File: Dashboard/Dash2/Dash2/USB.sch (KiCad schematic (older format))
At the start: 8 parts, among them J501 USB_B_Micro, U501 CP2102N-A01-GQFN24

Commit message: Add complete layout of the board
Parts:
- C501: Mouser Part Number (none) -> 80-C0805C475K3RAUTO
- C502: Mouser Part Number (none) -> 80-C0805C104K3R
- D501: Mouser Part Number (none) -> 576-SP0503BAHTG
- J501: Mouser Part Number (none) -> 538-105017-1001
- R501: Mouser Part Number (none) -> 71-CRCW0805-22.1K-E3
- R502: Mouser Part Number (none) -> 71-CRCW0805-47.5K-E3
- R503: Mouser Part Number (none) -> 71-CRCW08051K00FKEAC
- U501: Mouser Part Number (none) -> 634-CP2102NA01GQFN24
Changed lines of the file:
@@
 EESchema Schematic File Version 4
-LIBS:Dash2-cache
-EELAYER 26 0
+EELAYER 30 0
 EELAYER END
 $Descr A4 11693 8268
 encoding utf-8
-Sheet 5 4
+Sheet 4 4
 Title ""
 Date ""
@@
 F 2 "Package_DFN_QFN:QFN-24-1EP_4x4mm_P0.5mm_EP2.6x2.6mm" H 5950 3000 50  0001 L CNN
 F 3 "http://www.silabs.com/support%20documents/technicaldocs/cp2102n-datasheet.pdf" H 5550 2750 50  0001 C CNN
+F 4 "634-CP2102NA01GQFN24 " H 5500 3800 50  0001 C CNN "Mouser Part Number"
 	1    5500 3800
 	1    0    0    -1
@@
 F 3 "~" H 3150 4250 50  0001 C CNN
 F 4 "105017-1001" H 3000 4300 50  0001 C CNN "P/N"
+F 5 " 538-105017-1001 " H 3000 4300 50  0001 C CNN "Mouser Part Number"
 	1    3000 4300
 	1    0    0    -1
@@
 F 2 "Package_TO_SOT_SMD:SOT-143" H 4175 4750 50  0001 L CNN
 F 3 "http://www.littelfuse.com/~/media/files/littelfuse/technical%20resources/documents/data%20sheets/sp05xxba.pdf" H 4075 4925 50  0001 C CNN
+F 4 "576-SP0503BAHTG " H 3950 4800 50  0001 C CNN "Mouser Part Number"
 	1    3950 4800
 	1    0    0    -1
@@
 F 2 "Resistor_SMD:R_0805_2012Metric" V 4630 4500 50  0001 C CNN
 F 3 "~" H 4700 4500 50  0001 C CNN
+F 4 "71-CRCW0805-47.5K-E3" H 4700 4500 50  0001 C CNN "Mouser Part Number"
 	1    4700 4500
 	1    0    0    -1
@@
 F 2 "Resistor_SMD:R_0805_2012Metric" V 4280 4100 50  0001 C CNN
 F 3 "~" H 4350 4100 50  0001 C CNN
+F 4 "71-CRCW0805-22.1K-E3" H 4350 4100 50  0001 C CNN "Mouser Part Number"
 	1    4350 4100
 	0    1    1    0
@@
 F 2 "Resistor_SMD:R_0805_2012Metric" V 4730 3000 50  0001 C CNN
 F 3 "~" H 4800 3000 50  0001 C CNN
+F 4 "71-CRCW08051K00FKEAC" H 4800 3000 50  0001 C CNN "Mouser Part Number"
 	1    4800 3000
 	1    0    0    -1
@@
 F 2 "Capacitor_SMD:C_0805_2012Metric" H 5938 2650 50  0001 C CNN
 F 3 "~" H 5900 2800 50  0001 C CNN
+F 4 "80-C0805C475K3RAUTO " H 5900 2800 50  0001 C CNN "Mouser Part Number"
 	1    5900 2800
 	1    0    0    -1
@@
 F 2 "Capacitor_SMD:C_0805_2012Metric" H 6438 2650 50  0001 C CNN
 F 3 "~" H 6400 2800 50  0001 C CNN
+F 4 "80-C0805C104K3R " H 6400 2800 50  0001 C CNN "Mouser Part Number"
 	1    6400 2800
 	1    0    0    -1

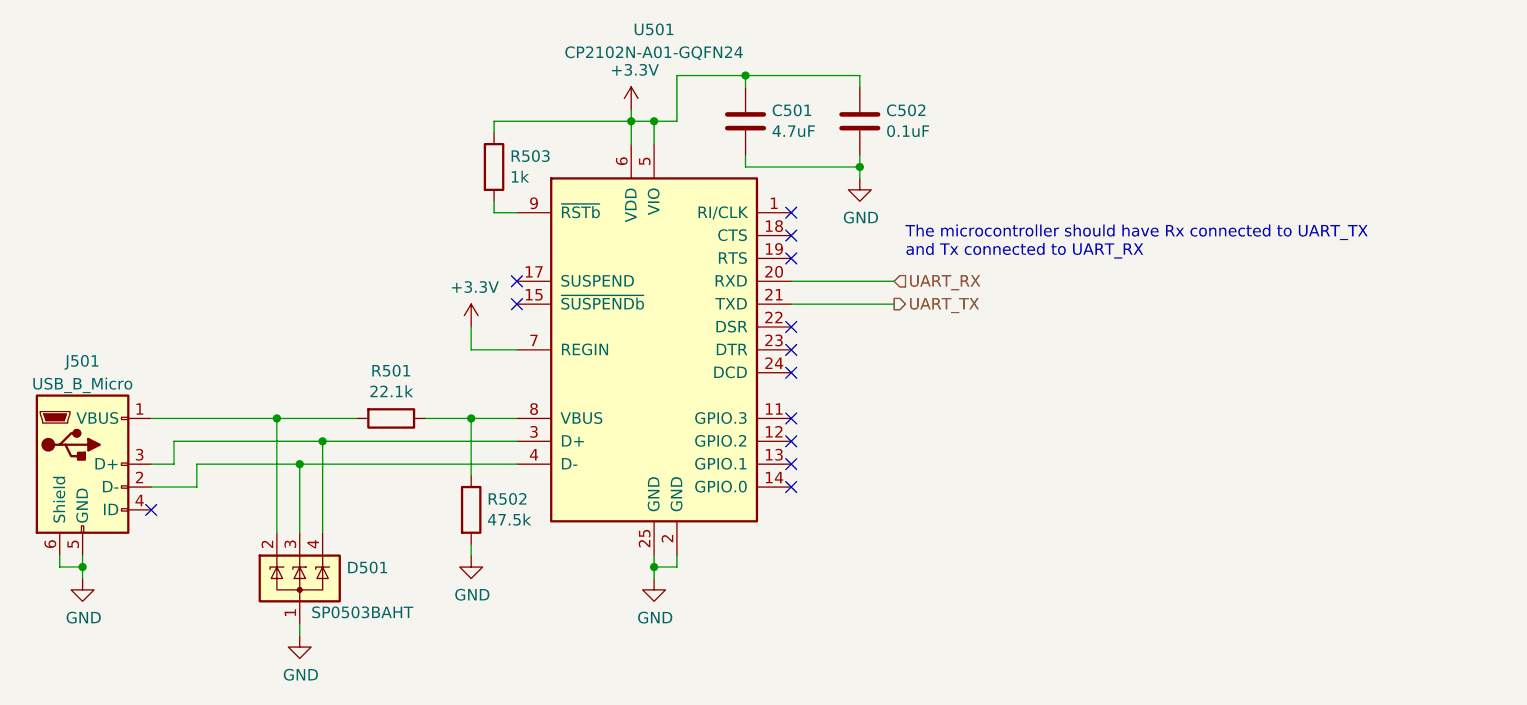
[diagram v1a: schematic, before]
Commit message: Add LED board and timing circuitry. The LED board is not yet integrated with the Dash.
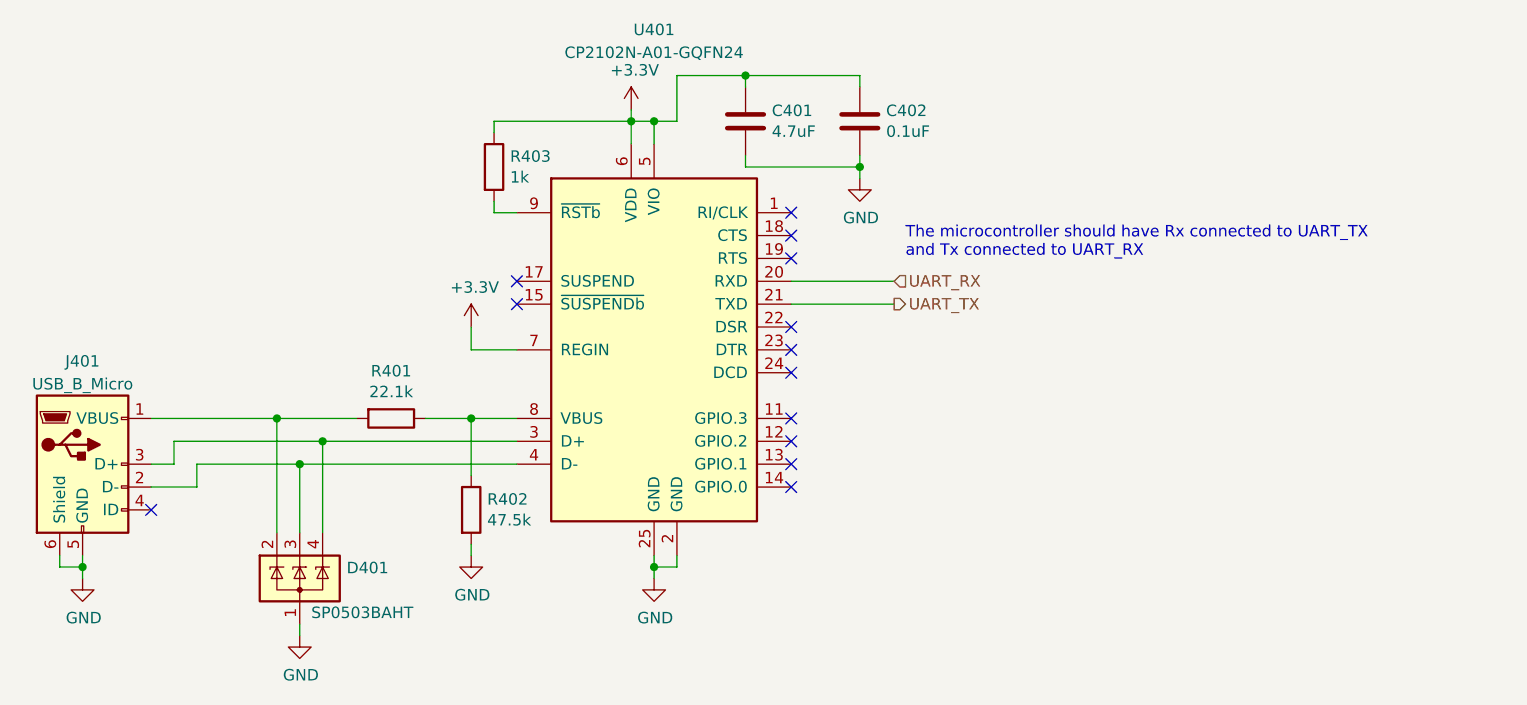
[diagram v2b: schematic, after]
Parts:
- renumbered C501 to C401, C502 to C402, D501 to D401, J501 to J401, R501 to R401, R502 to R402, R503 to R403, U501 to U401
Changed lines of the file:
@@
 $Descr A4 11693 8268
 encoding utf-8
-Sheet 4 4
+Sheet 4 6
 Title ""
 Date ""
@@
 $EndDescr
 $Comp
-L Interface_USB:CP2102N-A01-GQFN24 U501
+L Interface_USB:CP2102N-A01-GQFN24 U401
 U 1 1 5C4963B2
 P 5500 3800
-F 0 "U501" H 5500 5200 50  0000 C CNN
+F 0 "U401" H 5500 5200 50  0000 C CNN
 F 1 "CP2102N-A01-GQFN24" H 5500 5100 50  0000 C CNN
 F 2 "Package_DFN_QFN:QFN-24-1EP_4x4mm_P0.5mm_EP2.6x2.6mm" H 5950 3000 50  0001 L CNN
@@
 $EndComp
 $Comp
-L Connector:USB_B_Micro J501
+L Connector:USB_B_Micro J401
 U 1 1 5C4964BB
 P 3000 4300
-F 0 "J501" H 3000 4750 50  0000 C CNN
+F 0 "J401" H 3000 4750 50  0000 C CNN
 F 1 "USB_B_Micro" H 3000 4650 50  0000 C CNN
 F 2 "Connector_USB:USB_Micro-B_Molex-105017-0001" H 3150 4250 50  0001 C CNN
@@
 	3500 4400 3500 4300
 $Comp
-L power:GND #PWR0501
+L power:GND #PWR0401
 U 1 1 5C4965DF
 P 3000 4800
-F 0 "#PWR0501" H 3000 4550 50  0001 C CNN
+F 0 "#PWR0401" H 3000 4550 50  0001 C CNN
 F 1 "GND" H 3005 4627 50  0000 C CNN
 F 2 "" H 3000 4800 50  0001 C CNN
@@
 Connection ~ 3000 4750
 $Comp
-L power:GND #PWR0506
+L power:GND #PWR0406
 U 1 1 5C4966CF
 P 5500 4800
-F 0 "#PWR0506" H 5500 4550 50  0001 C CNN
+F 0 "#PWR0406" H 5500 4550 50  0001 C CNN
 F 1 "GND" H 5505 4627 50  0000 C CNN
 F 2 "" H 5500 4800 50  0001 C CNN
@@
 	5500 4750 5500 4800
 $Comp
-L Dash2-rescue:SP0503BAHT-Power_Protection D501
+L Dash2-rescue:SP0503BAHT-Power_Protection D401
 U 1 1 5C496C9B
 P 3950 4800
-F 0 "D501" H 4155 4846 50  0000 L CNN
+F 0 "D401" H 4155 4846 50  0000 L CNN
 F 1 "SP0503BAHT" H 4000 4650 50  0000 L CNN
 F 2 "Package_TO_SOT_SMD:SOT-143" H 4175 4750 50  0001 L CNN
@@
 $EndComp
 $Comp
-L power:GND #PWR0502
+L power:GND #PWR0402
 U 1 1 5C497074
 P 3950 5050
-F 0 "#PWR0502" H 3950 4800 50  0001 C CNN
+F 0 "#PWR0402" H 3950 4800 50  0001 C CNN
 F 1 "GND" H 3955 4877 50  0000 C CNN
 F 2 "" H 3950 5050 50  0001 C CNN
@@
 	3850 4600 3850 4100
 $Comp
-L Device:R R502
+L Device:R R402
 U 1 1 5C497DB9
 P 4700 4500
-F 0 "R502" H 4770 4546 50  0000 L CNN
+F 0 "R402" H 4770 4546 50  0000 L CNN
 F 1 "47.5k" H 4770 4455 50  0000 L CNN
 F 2 "Resistor_SMD:R_0805_2012Metric" V 4630 4500 50  0001 C CNN
@@
 $EndComp
 $Comp
-L Device:R R501
+L Device:R R401
 U 1 1 5C497DDB
 P 4350 4100
-F 0 "R501" V 4143 4100 50  0000 C CNN
+F 0 "R401" V 4143 4100 50  0000 C CNN
 F 1 "22.1k" V 4234 4100 50  0000 C CNN
 F 2 "Resistor_SMD:R_0805_2012Metric" V 4280 4100 50  0001 C CNN
@@
 	4200 4100 3850 4100
 $Comp
-L power:GND #PWR0504
+L power:GND #PWR0404
 U 1 1 5C498DBE
 P 4700 4700
-F 0 "#PWR0504" H 4700 4450 50  0001 C CNN
+F 0 "#PWR0404" H 4700 4450 50  0001 C CNN
 F 1 "GND" H 4705 4527 50  0000 C CNN
 F 2 "" H 4700 4700 50  0001 C CNN
@@
 	4700 4700 4700 4650
 $Comp
-L power:+3.3V #PWR0505
+L power:+3.3V #PWR0405
 U 1 1 5C499E7D
 P 5400 2750
-F 0 "#PWR0505" H 5400 2600 50  0001 C CNN
+F 0 "#PWR0405" H 5400 2600 50  0001 C CNN
 F 1 "+3.3V" H 5415 2923 50  0000 C CNN
 F 2 "" H 5400 2750 50  0001 C CNN
@@
 Connection ~ 5400 2800
 $Comp
-L Device:R R503
+L Device:R R403
 U 1 1 5C49B01B
 P 4800 3000
-F 0 "R503" H 4870 3046 50  0000 L CNN
+F 0 "R403" H 4870 3046 50  0000 L CNN
 F 1 "1k" H 4870 2955 50  0000 L CNN
 F 2 "Resistor_SMD:R_0805_2012Metric" V 4730 3000 50  0001 C CNN
@@
 	4800 2800 5400 2800
 $Comp
-L Device:C C501
+L Device:C C401
 U 1 1 5C49CC52
 P 5900 2800
-F 0 "C501" H 6015 2846 50  0000 L CNN
+F 0 "C401" H 6015 2846 50  0000 L CNN
 F 1 "4.7uF" H 6015 2755 50  0000 L CNN
 F 2 "Capacitor_SMD:C_0805_2012Metric" H 5938 2650 50  0001 C CNN
@@
 NoConn ~ 6100 4400
 $Comp
-L power:+3.3V #PWR0503
+L power:+3.3V #PWR0403
 U 1 1 5C4A2CBF
 P 4700 3700
-F 0 "#PWR0503" H 4700 3550 50  0001 C CNN
+F 0 "#PWR0403" H 4700 3550 50  0001 C CNN
 F 1 "+3.3V" H 4715 3873 50  0000 C CNN
 F 2 "" H 4700 3700 50  0001 C CNN
@@
 	4700 3800 4900 3800
 $Comp
-L Device:C C502
+L Device:C C402
 U 1 1 5C4A4791
 P 6400 2800
-F 0 "C502" H 6515 2846 50  0000 L CNN
+F 0 "C402" H 6515 2846 50  0000 L CNN
 F 1 "0.1uF" H 6515 2755 50  0000 L CNN
 F 2 "Capacitor_SMD:C_0805_2012Metric" H 6438 2650 50  0001 C CNN
@@
 $EndComp
 $Comp
-L power:GND #PWR0507
+L power:GND #PWR0407
 U 1 1 5C4A4BE4
 P 6400 3050
-F 0 "#PWR0507" H 6400 2800 50  0001 C CNN
+F 0 "#PWR0407" H 6400 2800 50  0001 C CNN
 F 1 "GND" H 6405 2877 50  0000 C CNN
 F 2 "" H 6400 3050 50  0001 C CNN
